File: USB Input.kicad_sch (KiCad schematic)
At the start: 6 parts, among them J602 1051640001, U601 ESD Protection IC

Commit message: Updated symbols, added jobset and output folders.
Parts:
- R603, R604: Manufacturer (none) -> UNI-ROYAL(Uniroyal Elec); Manufacturer Part No (none) -> 0805W8F1003T5E
- TP601: now left out of the parts list
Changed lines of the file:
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@@
 		(unit 1)
 		(exclude_from_sim no)
-		(in_bom yes)
+		(in_bom no)
 		(on_board yes)
 		(dnp no)
@@
 			)
 		)
+		(property "Manufacturer" "UNI-ROYAL(Uniroyal Elec)"
+			(at 241.3 757.15 0)
+			(effects
+				(font
+					(size 1.27 1.27)
+				)
+				(justify left top)
+				(hide yes)
+			)
+		)
+		(property "Manufacturer Part No" "0805W8F1003T5E"
+			(at 241.3 857.15 0)
+			(effects
+				(font
+					(size 1.27 1.27)
+				)
+				(justify left top)
+				(hide yes)
+			)
+		)
 		(pin "2"
 		)
@@
 				(hide yes)
 			)
+		)
+		(property "Manufacturer" "UNI-ROYAL(Uniroyal Elec)"
+			(at 214.63 757.15 0)
+			(effects
+				(font
+					(size 1.27 1.27)
+				)
+				(justify left top)
+				(hide yes)
+			)
+		)
+		(property "Manufacturer Part No" "0805W8F1003T5E"
+			(at 214.63 857.15 0)
+			(effects
+				(font
+					(size 1.27 1.27)
+				)
+				(justify left top)
+				(hide yes)
+			)

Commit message: Updated inductor component and 10uF capacitor components to bring down cost.
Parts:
- renumbered J602 to J601, R603 to R601, R604 to R602
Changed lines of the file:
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@@
 		(dnp no)
 		(fields_autoplaced yes)
-		(property "Reference" "R604"
+		(property "Reference" "R602"
 			(at 232.41 54.61 0)
 			(effects
@@
 			(project ""
 				(path "/fb66fec7-a625-41b0-8b4b-639a0ec63be1/8cb1b373-89d4-44fe-a70d-44b57920bc78"
-					(reference "R604")
+					(reference "R602")
 					(unit 1)
 				)
@@
 		(dnp no)
 		(fields_autoplaced yes)
-		(property "Reference" "R603"
+		(property "Reference" "R601"
 			(at 205.74 54.61 0)
 			(effects
@@
 			(project "MQTT-ModularControllerBoard"
 				(path "/fb66fec7-a625-41b0-8b4b-639a0ec63be1/8cb1b373-89d4-44fe-a70d-44b57920bc78"
-					(reference "R603")
+					(reference "R601")
 					(unit 1)
 				)
@@
 		(dnp no)
 		(fields_autoplaced yes)
-		(property "Reference" "J602"
+		(property "Reference" "J601"
 			(at 75.5332 87.63 0)
 			(effects
@@
 			(project ""
 				(path "/fb66fec7-a625-41b0-8b4b-639a0ec63be1/8cb1b373-89d4-44fe-a70d-44b57920bc78"
-					(reference "J602")
+					(reference "J601")
 					(unit 1)
 				)

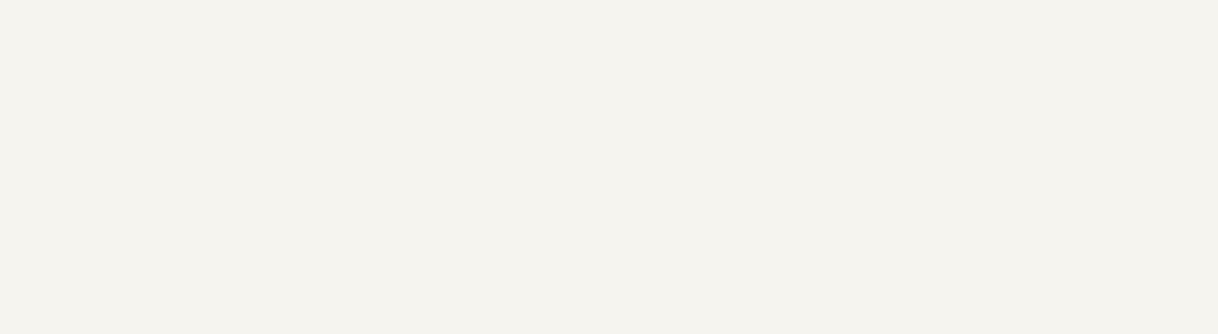
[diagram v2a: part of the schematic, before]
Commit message: Updated the input diode to a TVS that is in stock/normally stocked by JLCPCB
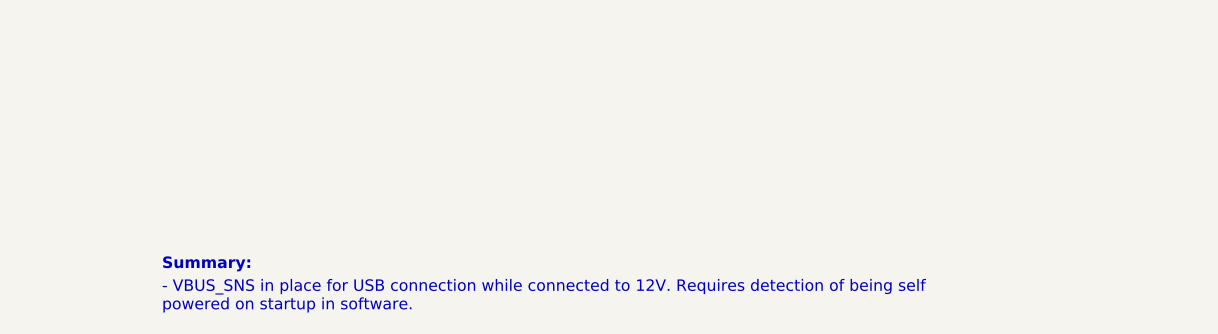
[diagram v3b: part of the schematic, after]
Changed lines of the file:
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@@
+		)
+	)
+	(text_box "Summary:"
+		(exclude_from_sim no)
+		(at 177.8 166.37 0)
+		(size 20.32 3.81)
+		(margins 0.9525 0.9525 0.9525 0.9525)
+		(stroke
+			(width -0.0001)
+			(type solid)
+		)
+		(fill
+			(type none)
+		)
+		(effects
+			(font
+				(size 1.27 1.27)
+				(thickness 0.254)
+				(bold yes)
+			)
+			(justify left top)
 		)
 	)
@@
 		(margins 0.9525 0.9525 0.9525 0.9525)
 		(stroke
+			(width -0.0001)
+			(type solid)
+		)
+		(fill
+			(type none)
+		)
+		(effects
+			(font
+				(size 1.27 1.27)
+			)
+			(justify left top)
+		)
+	)
+	(text_box "- VBUS_SNS in place for USB connection while connected to 12V. Requires detection of being self powered on startup in software."
+		(exclude_from_sim no)
+		(at 177.8 168.91 0)
+		(size 102.87 11.43)
+		(margins 0.9525 0.9525 0.9525 0.9525)
+		(stroke
